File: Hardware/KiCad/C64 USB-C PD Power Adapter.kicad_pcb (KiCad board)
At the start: 2 copper layers, 46.1 x 30 mm, 41 parts, among them J1 USB-C (power in), J2 C64 POWER (DIN-7 male), Q1 AO3401A, U1 CH224A, U2 TPS54302DDCR, U3 TPS54302DDCR

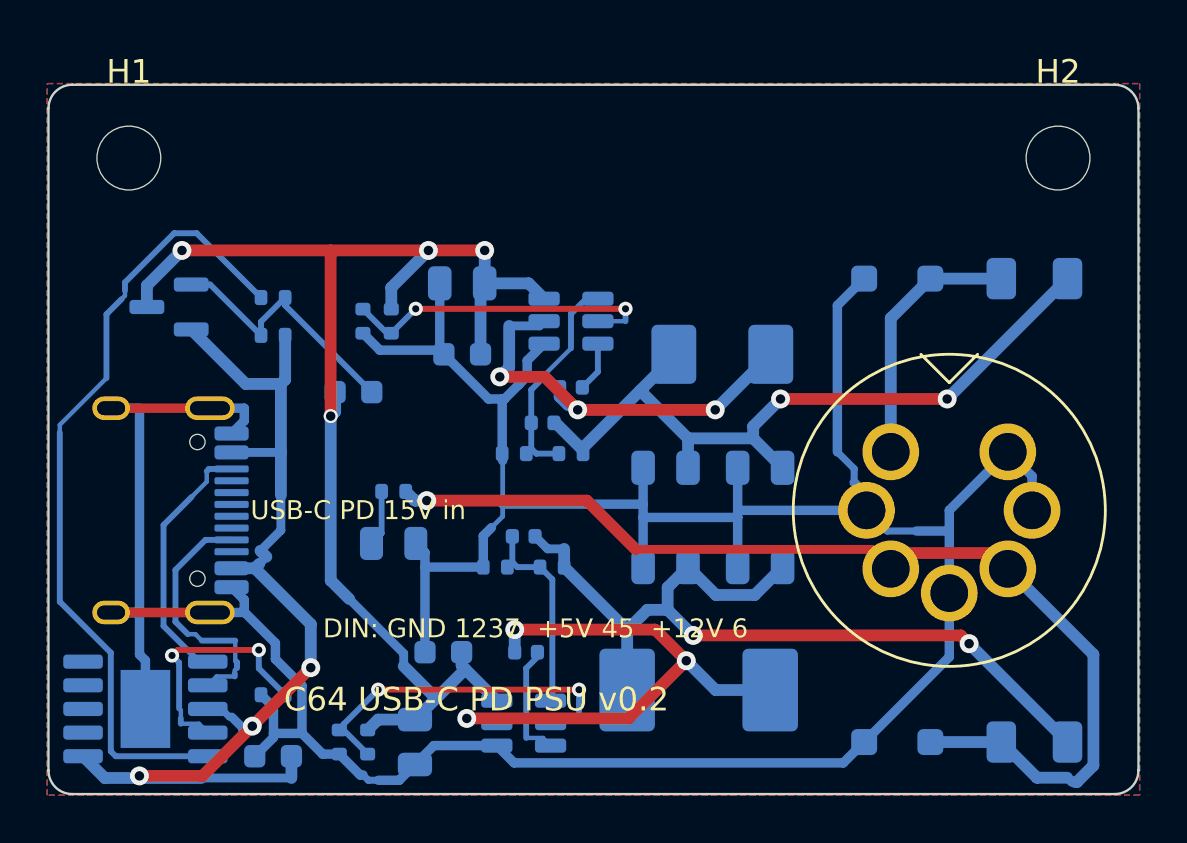
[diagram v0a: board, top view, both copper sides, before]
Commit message: v0.3: cut JLC extended parts from 15 to 4, 0603 passives
All 0402 parts moved to 0603 JLC Basic; TVS diodes swapped to Preferred
parts; L1 now the same FXL0530 as L2; PTCs replaced by Basic 0R links
(footprints still take a 1206 PTC); 5 V feedback 75k/10k. Board rebuilt
from the user's placement, re-routed (DRC clean). CPL now carries the
U1-U3 +90 fix confirmed in JLC's preview.

Co-Authored-By: Claude Opus 5.5 <noreply@anthropic.com>
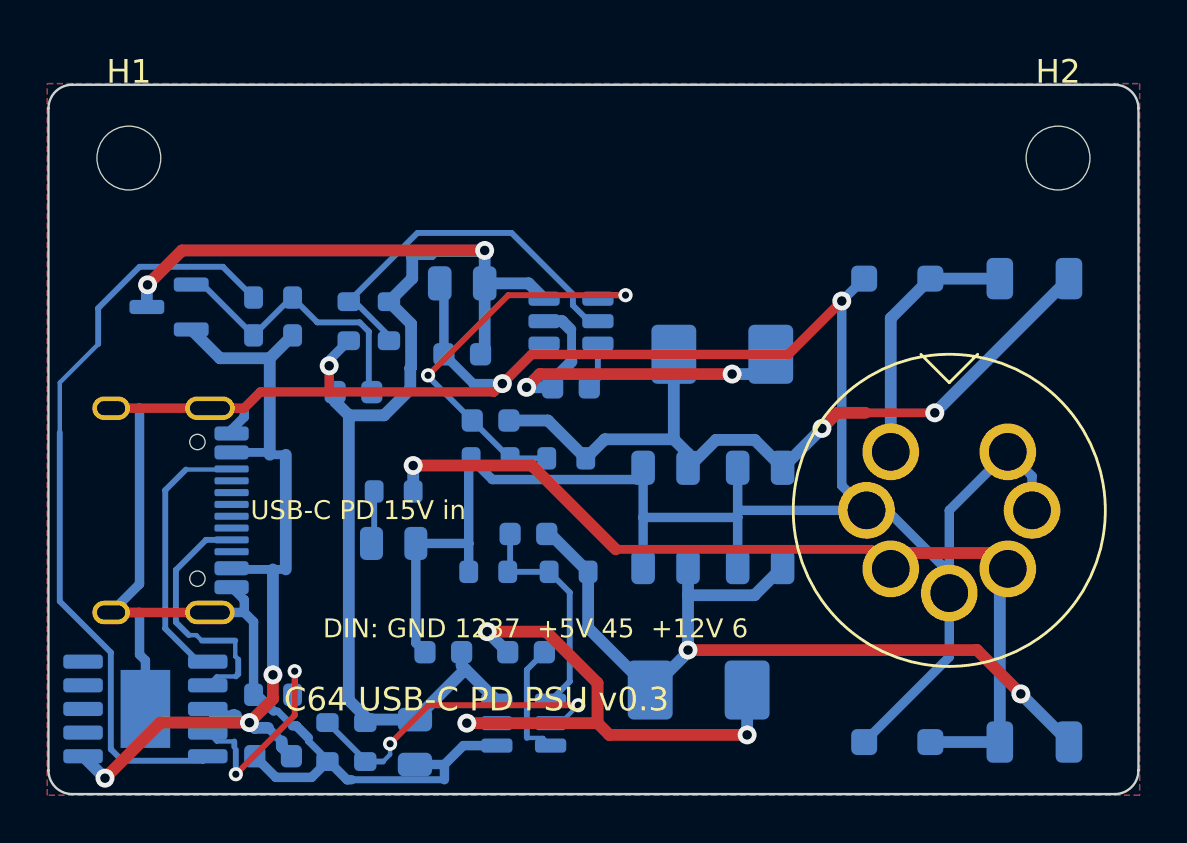
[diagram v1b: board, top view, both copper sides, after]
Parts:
- C11, C5: value 100nF -> 100nF/50V; footprint C64_PD_PSU:C_0402_1005Metric -> C64_PD_PSU:C_0603_1608Metric
- C14, C8: value 75pF -> 100pF; footprint C64_PD_PSU:C_0402_1005Metric -> C64_PD_PSU:C_0603_1608Metric
- F1: value 2A -> 0R; footprint C64_PD_PSU:Fuse_1206_3216Metric -> C64_PD_PSU:R_1206_3216Metric
- F2: value 1.1A -> 0R; footprint C64_PD_PSU:Fuse_1206_3216Metric -> C64_PD_PSU:R_1206_3216Metric
- L1: footprint C64_PD_PSU:L_Changjiang_FXL0630 -> C64_PD_PSU:L_Changjiang_FXL0530
- R1, R10, R11, R12, R2, R3, R4, R5, R8, R9: footprint C64_PD_PSU:R_0402_1005Metric -> C64_PD_PSU:R_0603_1608Metric
- R6: value 100k -> 75k; footprint C64_PD_PSU:R_0402_1005Metric -> C64_PD_PSU:R_0603_1608Metric
- R7: value 13.3k -> 10k; footprint C64_PD_PSU:R_0402_1005Metric -> C64_PD_PSU:R_0603_1608Metric
- moved C14 2.20 mm to (119.6, 109.2)
- moved R12 1.02 mm to (119.6, 110.8)
- moved R6 0.73 mm to (122.9, 115.6)
- moved R10 0.60 mm to (113.6, 105.0)
- moved R5 0.50 mm to (112.7, 122.8)
- moved R7 0.36 mm to (119.5, 115.6)
- moved R11 0.28 mm to (122.8, 110.8)
- moved C8 0.22 mm to (121.2, 114.0)
- moved R4 0.10 mm to (114.3, 122.8)
- moved R9 0.10 mm to (115.3, 105.0)
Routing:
- net GND: track 150.4 -> 161.0 mm, vias 0 -> 3
- net /FB2: track 9.35 -> 17.5 mm, vias 0 -> 2
- net VBUS: track 45.3 -> 38.5 mm
- net +5V: track 45.1 -> 39.0 mm
- net /EN2: track 13.7 -> 16.1 mm, vias 2 -> 0
- net /SW2: track 18.3 -> 16.1 mm, vias 3 -> 2
- net /VSW: track 55.9 -> 57.9 mm, vias 4 -> 2
- net /PG: track 33.8 -> 32.4 mm
- net /CFG1: track 10.5 -> 9.11 mm
- net /12V_BUCK: track 32.5 -> 33.4 mm
- net /FB: track 8.54 -> 9.48 mm
- net /GATE: track 11.4 -> 12.3 mm
- net /EN: track 14.9 -> 14.1 mm
- net /SW: track 24.5 -> 23.7 mm
- net /CC2: track 10.9 -> 11.4 mm
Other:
- board text added: "C64 USB-C PD PSU v0.3"
- board text removed: "C64 USB-C PD PSU v0.2"
